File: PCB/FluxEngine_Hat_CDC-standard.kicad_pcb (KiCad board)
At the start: 2 copper layers, 83.3 x 24.1 mm, 8 parts, among them J1 CY8CKIT-059, J2 Screw_Terminal_01x04, P1 FDC_BUS_IBMPC, P2 FDC_BUS_CDC_9406_STD, U1 LVC1G19

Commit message: reduce thermal spoke width
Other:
- board text added: "DC-IN 2A"
- board text removed: "DC IN, 2A"

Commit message: rotate 1G19 for easier hand soldering
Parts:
- U1: value LVC1G19 -> 1G19
- moved U1 0.68 mm to (106.4, 97.9), turned to 0 degrees
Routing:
- net /~{STEP_IN}: track 5.36 -> 7.35 mm
- net VCC: track 14.6 -> 16.2 mm
- net /~{STEP}: track 68.4 -> 69.7 mm
- net /DIRECTION: track 63.8 -> 64.9 mm
- net /~{STEP_OUT}: track 9.76 -> 10.3 mm

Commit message: CDC-standard traces to U1
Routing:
- net /DIR/~{STEP_IN}: track 55.1 -> 53.1 mm
- net /~{STEP}/~{STEP_OUT}: track 67.1 -> 66.0 mm
- net /~{STEP_IN}: track 7.35 -> 7.38 mm, vias 1 -> 0
- net GND: vias 37 -> 35

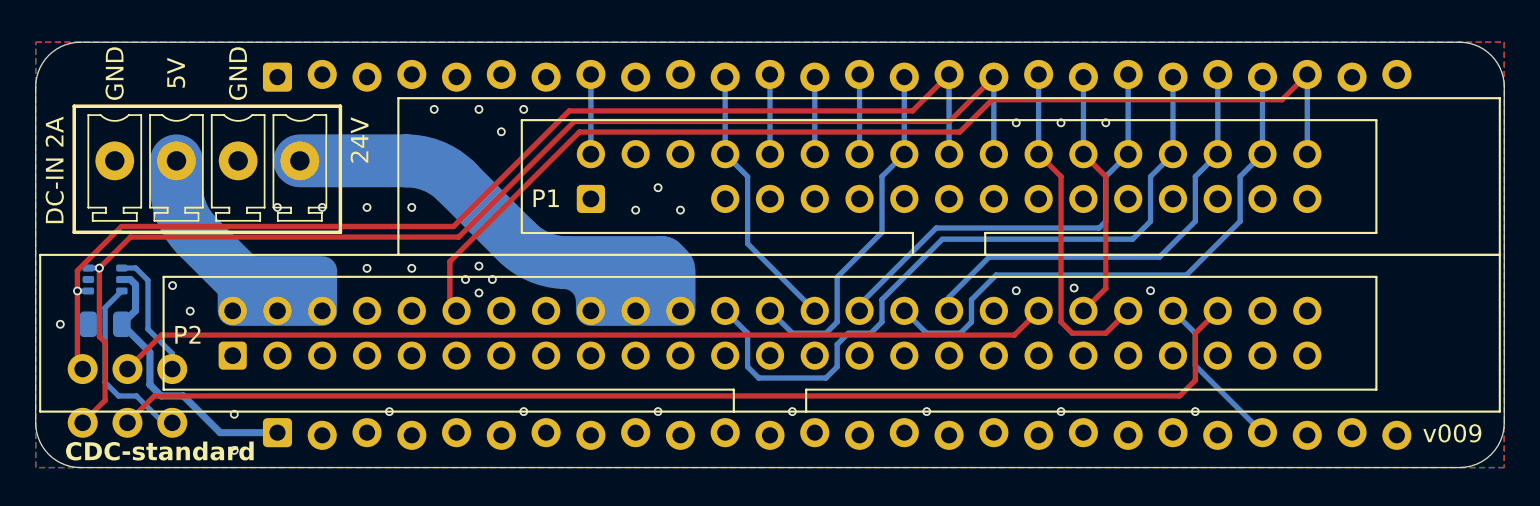
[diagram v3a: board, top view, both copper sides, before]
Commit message: staggered rows offset & direction
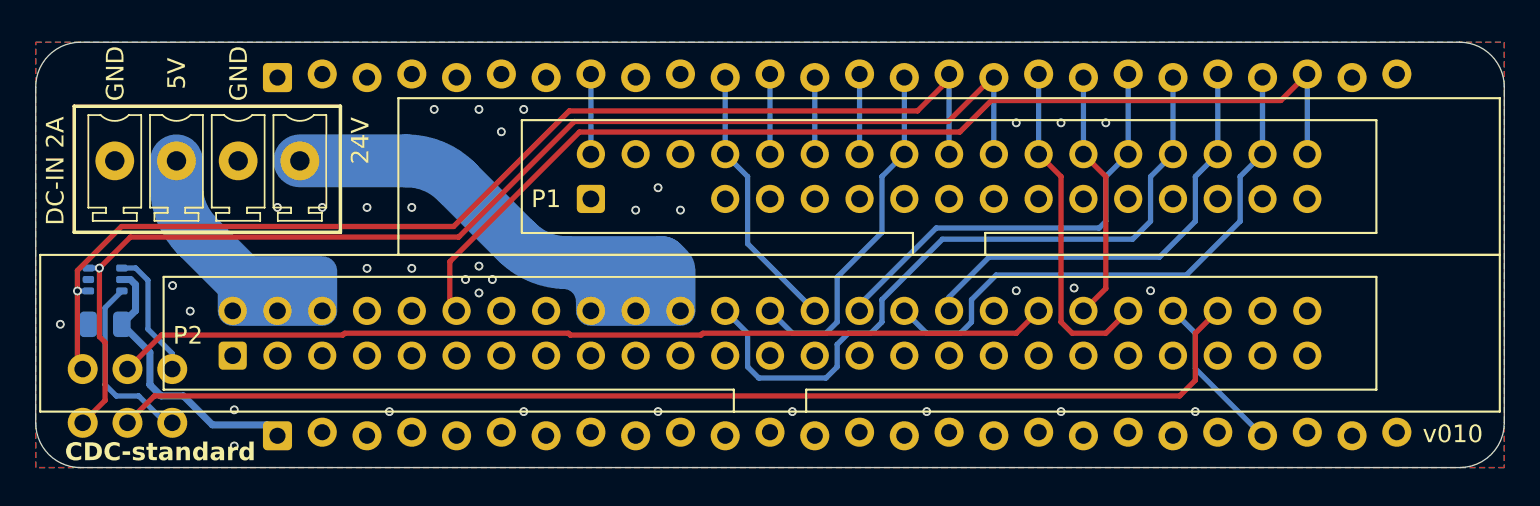
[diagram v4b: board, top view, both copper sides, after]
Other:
- board text added: "CY8CKIT-059 this side face up"
- board text removed: "CY8CKIT-059 usb & button face away from hat"
